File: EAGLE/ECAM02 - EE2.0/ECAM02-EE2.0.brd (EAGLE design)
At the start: 82.6 x 75.9 mm, 61 parts, among them J1 MODULAR TOOL, J2 SPI, J3 MOT, J4 FTDI, J5 S4B-PH-SM4, J6 SOL+PUMP, J7 RINGLIGHT, Q2 16MHz, U1 SP3485, U10 MCP4725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

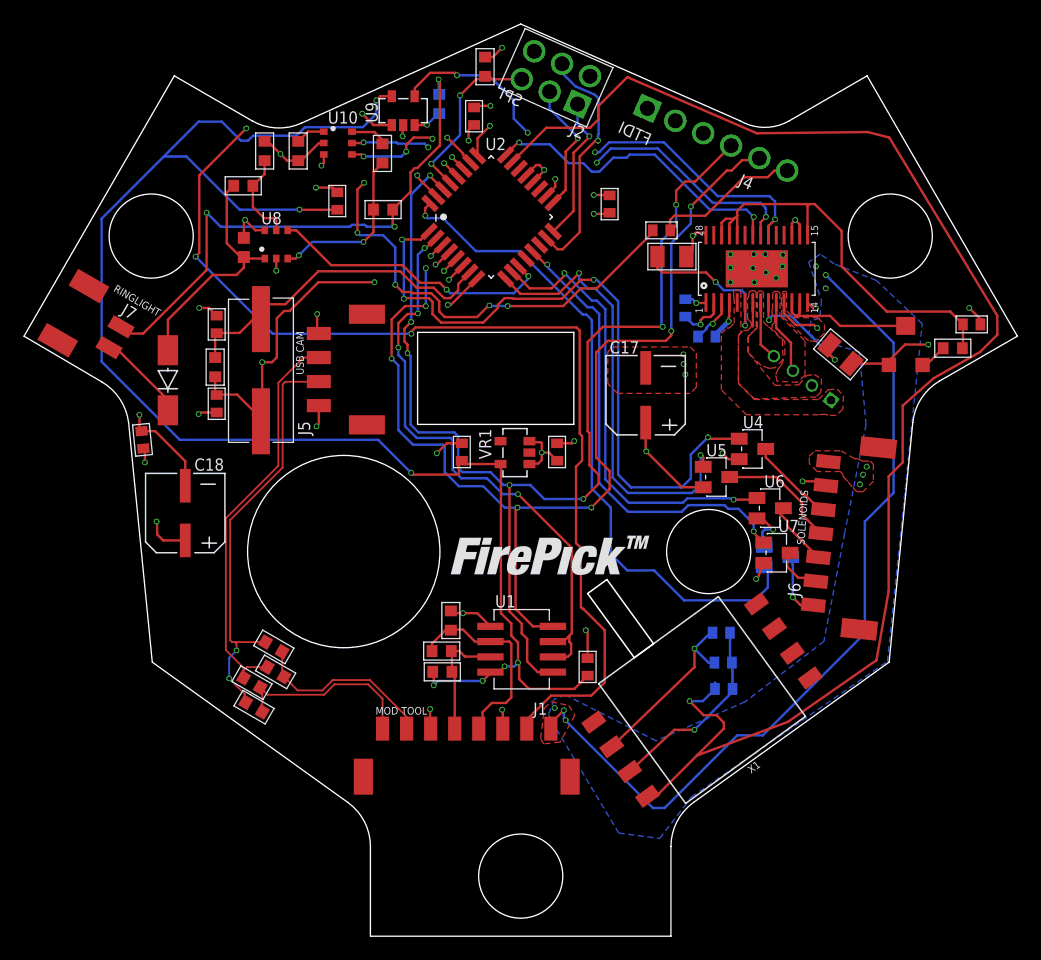
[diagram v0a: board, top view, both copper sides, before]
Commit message: Re-jiggered switching power supply for LED controller.  Re-routed and whatnot.  Generated GERBERs for REV--
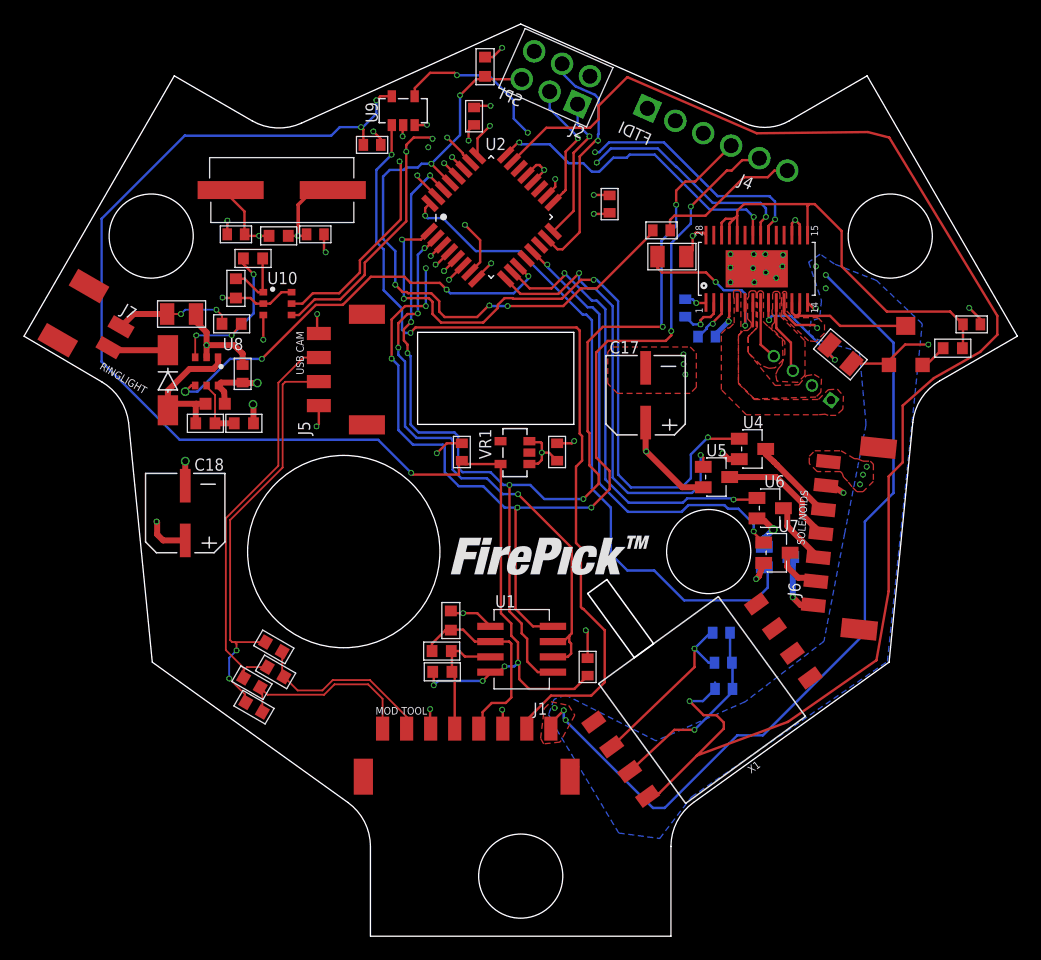
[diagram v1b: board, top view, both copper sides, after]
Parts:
- R17: value 10R -> 10R 1/4W; device TinWhiskers:R0603 -> TinWhiskers:R1206
- moved R17 27.7 mm to (13.1, 51.8), flipped to the top, turned to 180 degrees
- moved R16 22.7 mm to (18.3, 42.7), turned to 180 degrees
- moved R15 20.0 mm to (15.1, 42.7)
- moved C5 16.3 mm to (24.2, 58.4), turned to 180 degrees
- moved R18 15.8 mm to (17.3, 51.0), turned to 180 degrees
- moved Q2 15.1 mm to (21.4, 62.1), turned to 0 degrees
- moved U10 14.3 mm to (21.1, 52.6)
- moved R19 13.9 mm to (19.1, 56.4), turned to 180 degrees
- moved L1 13.2 mm to (15.9, 44.3), turned to 180 degrees
- moved R20 12.5 mm to (17.6, 53.9)
- moved R8 12.1 mm to (21.2, 58.3), turned to 0 degrees
- moved U8 12.0 mm to (15.2, 47.0), turned to 0 degrees
- moved C12 9.98 mm to (18.2, 46.8), turned to 270 degrees
- moved C4 7.66 mm to (17.6, 58.4), turned to 0 degrees
- moved C16 5.50 mm to (29.0, 65.8), turned to 180 degrees
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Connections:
- net N$1 renamed LED_ANODE
- net N$2 renamed LED_SW
- net N$3 renamed LED_CATHODE
- net N$4 renamed LED_FB
- net OV renamed LED_OV
- removed net A0: R19.1, U10.6
- net GND: now also U10.6
- net N$10: now also R19.1
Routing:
- net LED_CATHODE: track 46.1 -> 9.88 mm, vias 3 -> 2
- net !ENBL_MOD: track 100.2 -> 72.7 mm, vias 4 -> 2
- net +3V3: track 130.7 -> 114.7 mm
- net SDA: track 11.5 -> 25.9 mm, vias 4 -> 3
- net SCL: track 9.93 -> 23.7 mm
- net CTRL: track 24.1 -> 36.0 mm, vias 2 -> 4
- net XTAL2: track 36.3 -> 28.2 mm, vias 3 -> 2
- net LED_SW: track 20.2 -> 12.3 mm
- net RESET: track 60.3 -> 55.0 mm, vias 7 -> 5
- net GND: track 88.1 -> 93.1 mm
- net +5V: track 51.0 -> 47.1 mm
- net A0: track 3.14 -> 0.00 mm
- net N$10: track 2.46 -> 5.58 mm
- net XTAL1: track 26.9 -> 30.0 mm, vias 0 -> 2
- net LED_ANODE: track 7.52 -> 4.99 mm
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
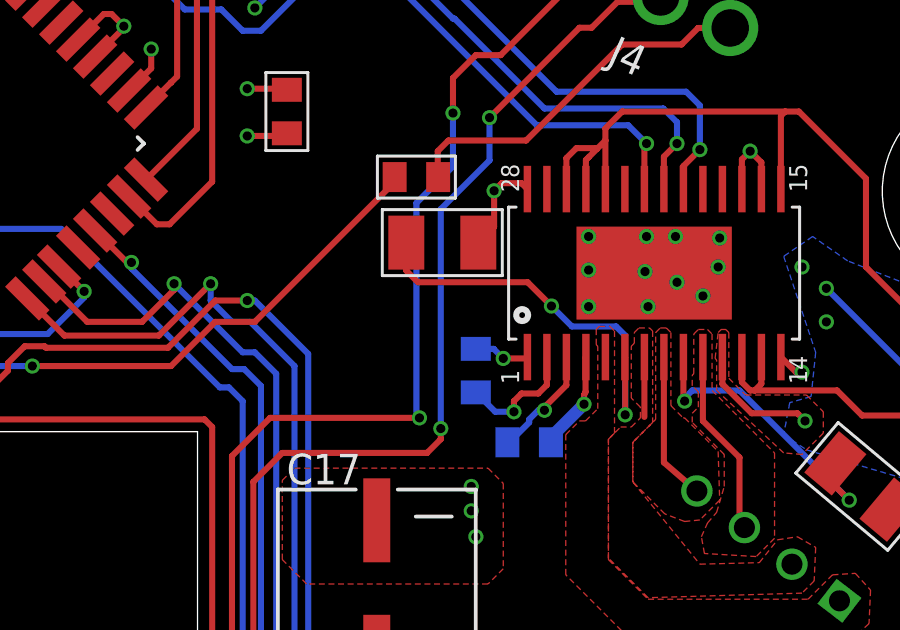
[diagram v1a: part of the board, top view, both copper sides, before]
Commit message: BOMs complete for all FPD boards
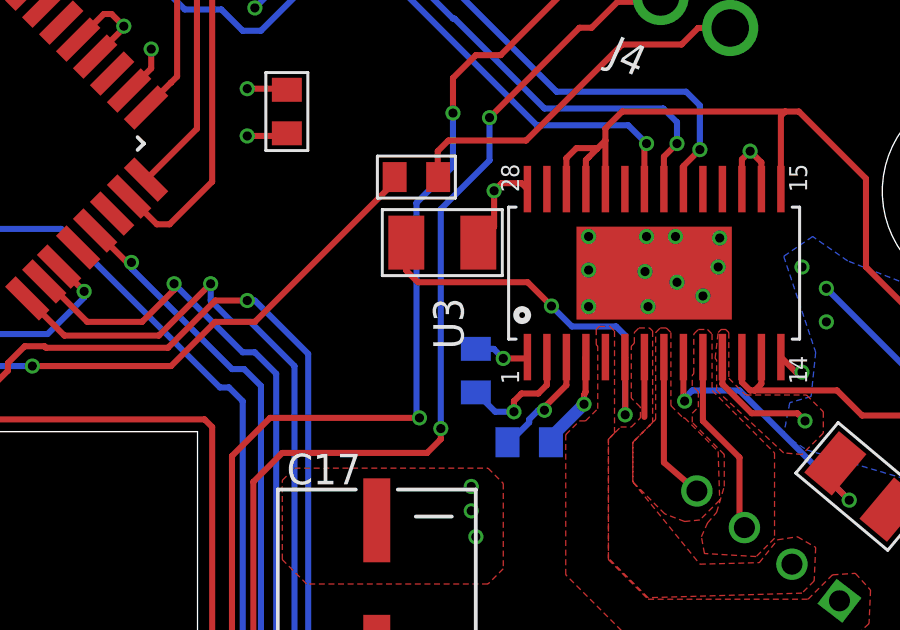
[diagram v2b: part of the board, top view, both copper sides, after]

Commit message: BOMs finished, inventory sheet created.
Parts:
- R2: value 100R -> 120R
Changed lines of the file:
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@@
 <attribute name="PARTNO" value="RC0603JR-070RL" x="18.288" y="42.672" size="1.778" layer="27" rot="R180" display="off"/>
 </element>
-<element name="R2" library="TinWhiskers" package="R0603" value="100R" x="34.7472" y="23.7236" smashed="yes">
-<attribute name="PARTNO" value="RC0603FR-07100RL" x="34.7472" y="23.7236" size="1.778" layer="27" display="off"/>
+<element name="R2" library="TinWhiskers" package="R0603" value="120R" x="34.7472" y="23.7236" smashed="yes">
+<attribute name="PARTNO" value="RC0603FR-07120RL" x="34.7472" y="23.7236" size="1.778" layer="27" display="off"/>
 <attribute name="NAME" x="31.414" y="23.2536" size="1.016" layer="51" font="vector" ratio="12"/>
 <attribute name="VALUE" x="36.6972" y="23.2736" size="1" layer="27" font="vector" ratio="10"/>
